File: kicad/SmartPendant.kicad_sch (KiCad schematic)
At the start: 51 parts, among them J1 UART, J2 ST-LINK, J3 Encoder, J5 Display, J6 USB_C_Receptacle_USB2.0_16P, J8 Micro_SD_Card_Det1, Q1 MMBT3904, U1 WEACT BLACKPILL F4X1, U2 AMS1117-3.3, U3 MB85RC256VPNF-G-JNERE1

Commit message: Route some more.
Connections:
- net USR_BTN: now also BTN_USR1.2; no longer BTN_USR1.1
- net at BTN_USR1.SH (B): now also BTN_USR1.1; no longer BTN_USR1.2
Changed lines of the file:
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@@
 		(lib_id "Switch:SW_Push_Shielded")
 		(at 209.55 172.72 0)
+		(mirror y)
 		(unit 1)
 		(exclude_from_sim no)
@@
 		(dnp no)
 		(property "Reference" "BTN_USR1"
-			(at 214.7316 164.0459 0)
+			(at 204.3684 164.0459 0)
 			(effects
 				(font
@@
 		)
 		(property "Value" "SPST"
-			(at 220.091 166.7891 0)
+			(at 199.009 166.7891 0)
 			(effects
 				(font

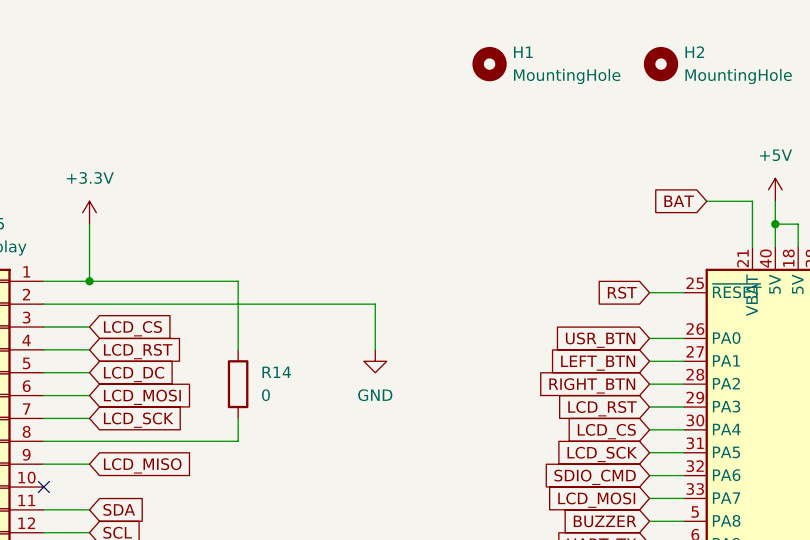
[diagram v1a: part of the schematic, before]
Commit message: Add GND test point.
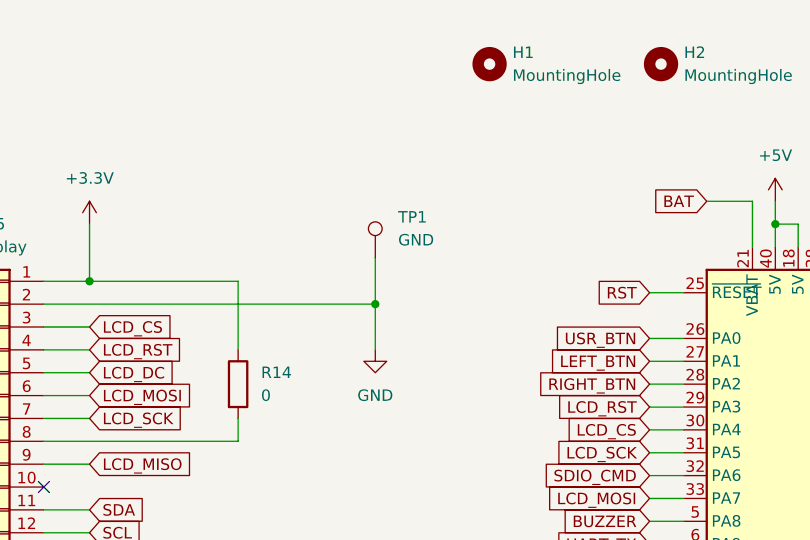
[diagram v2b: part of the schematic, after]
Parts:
- added TP1: GND, TestPoint:TestPoint_Keystone_5000-5004_Miniature, symbol Connector:TestPoint
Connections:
- net GND: now also TP1.1
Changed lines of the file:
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@@
 	)
 	(junction
+		(at 67.31 49.53)
+		(diameter 0)
+		(color 0 0 0 0)
+	)
+	(junction
 		(at 241.3 166.37)
 		(diameter 0)
@@
 	(wire
 		(pts
+			(xy 67.31 44.45) (xy 67.31 49.53)
+		)
+		(stroke
+			(width 0)
+			(type default)
+		)
+	)
+	(wire
+		(pts
 			(xy 241.3 165.1) (xy 241.3 166.37)
 		)
@@
 					(unit 1)
 				)
+			)
+		)
+	)
+	(symbol
+		(lib_id "Connector:TestPoint")
+		(at 67.31 44.45 0)
+		(unit 1)
+		(exclude_from_sim no)
+		(in_bom yes)
+		(on_board yes)
+		(dnp no)
+		(fields_autoplaced yes)
+		(property "Reference" "TP1"
+			(at 69.85 39.8779 0)
+			(effects
+				(font
+					(size 1.27 1.27)
+				)
+				(justify left)
+			)
+		)
+		(property "Value" "GND"
+			(at 69.85 42.4179 0)
+			(effects
+				(font
+					(size 1.27 1.27)
+				)
+				(justify left)
+			)
+		)
+		(property "Footprint" "TestPoint:TestPoint_Keystone_5000-5004_Miniature"
+			(at 72.39 44.45 0)
+			(effects
+				(font
+					(size 1.27 1.27)
+				)
+				(hide yes)
+			)
+		)
+		(property "Datasheet" "~"
+			(at 72.39 44.45 0)
+			(effects
+				(font
+					(size 1.27 1.27)
+				)
+				(hide yes)
+			)
+		)
+		(property "Description" "test point"
+			(at 67.31 44.45 0)
+			(effects
+				(font
+					(size 1.27 1.27)
+				)
+				(hide yes)
+			)
+		)
+		(pin "1"
+		)
+		(instances
+			(project ""
+				(path "/78cb6519-38e9-49e2-a9df-0cb5fdb5035f"
+					(reference "TP1")
+					(unit 1)
+				)

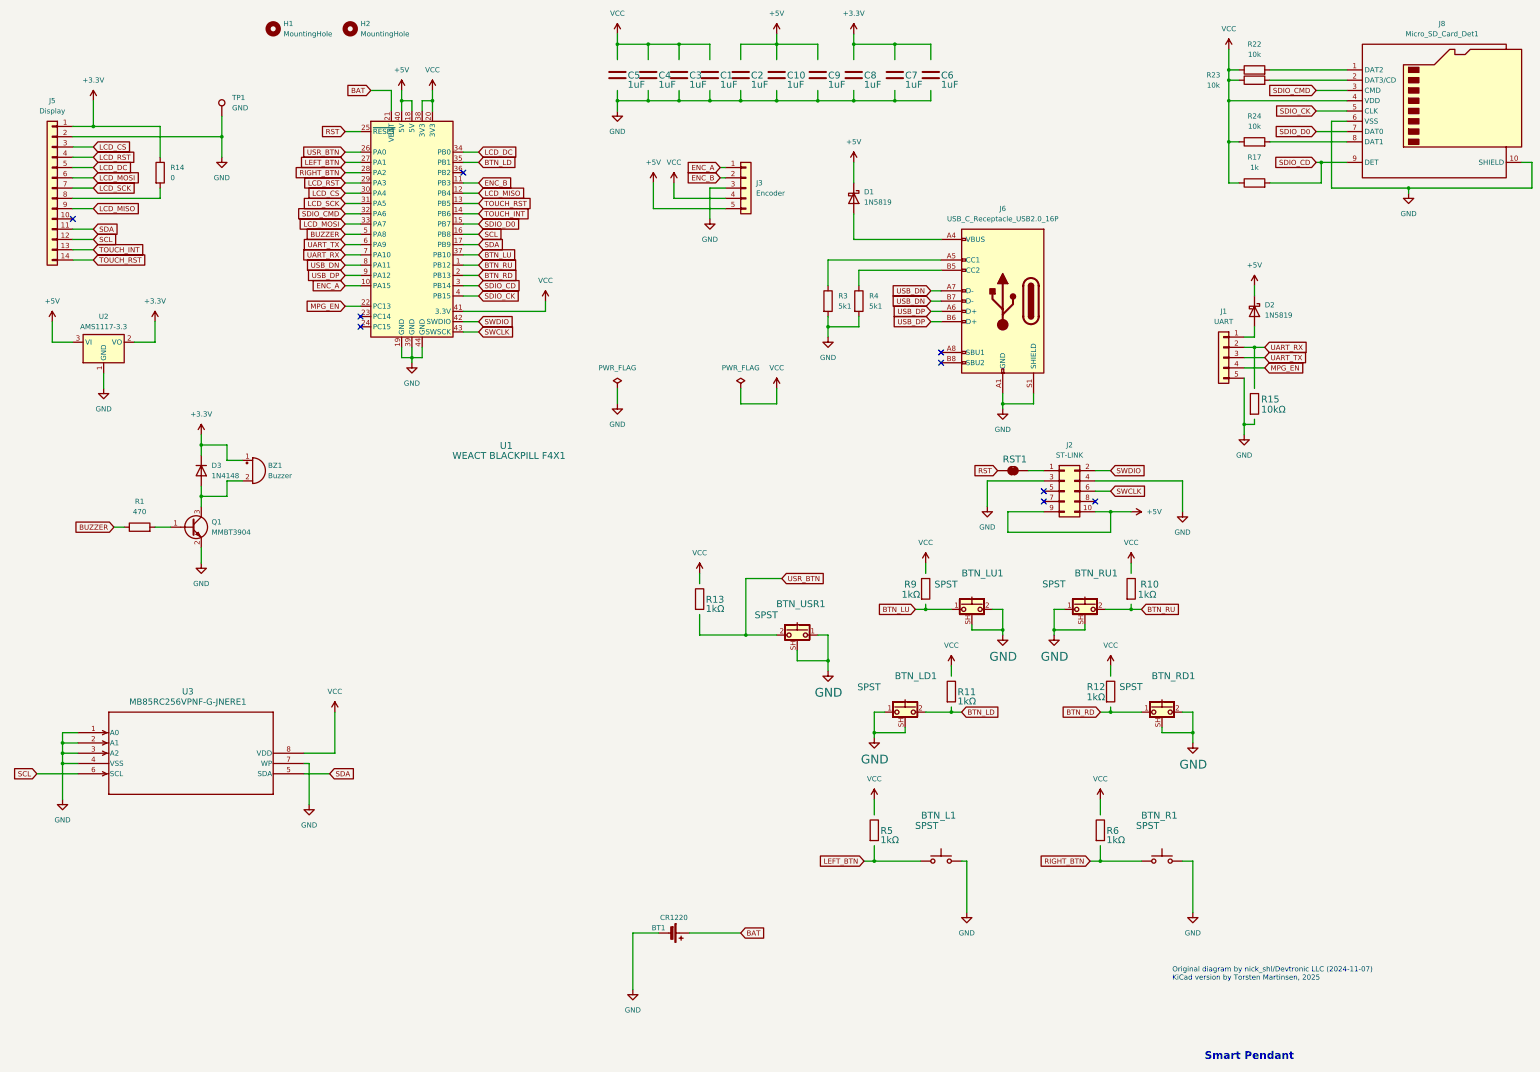
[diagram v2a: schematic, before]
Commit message: Use resistor array; make references consecutive.
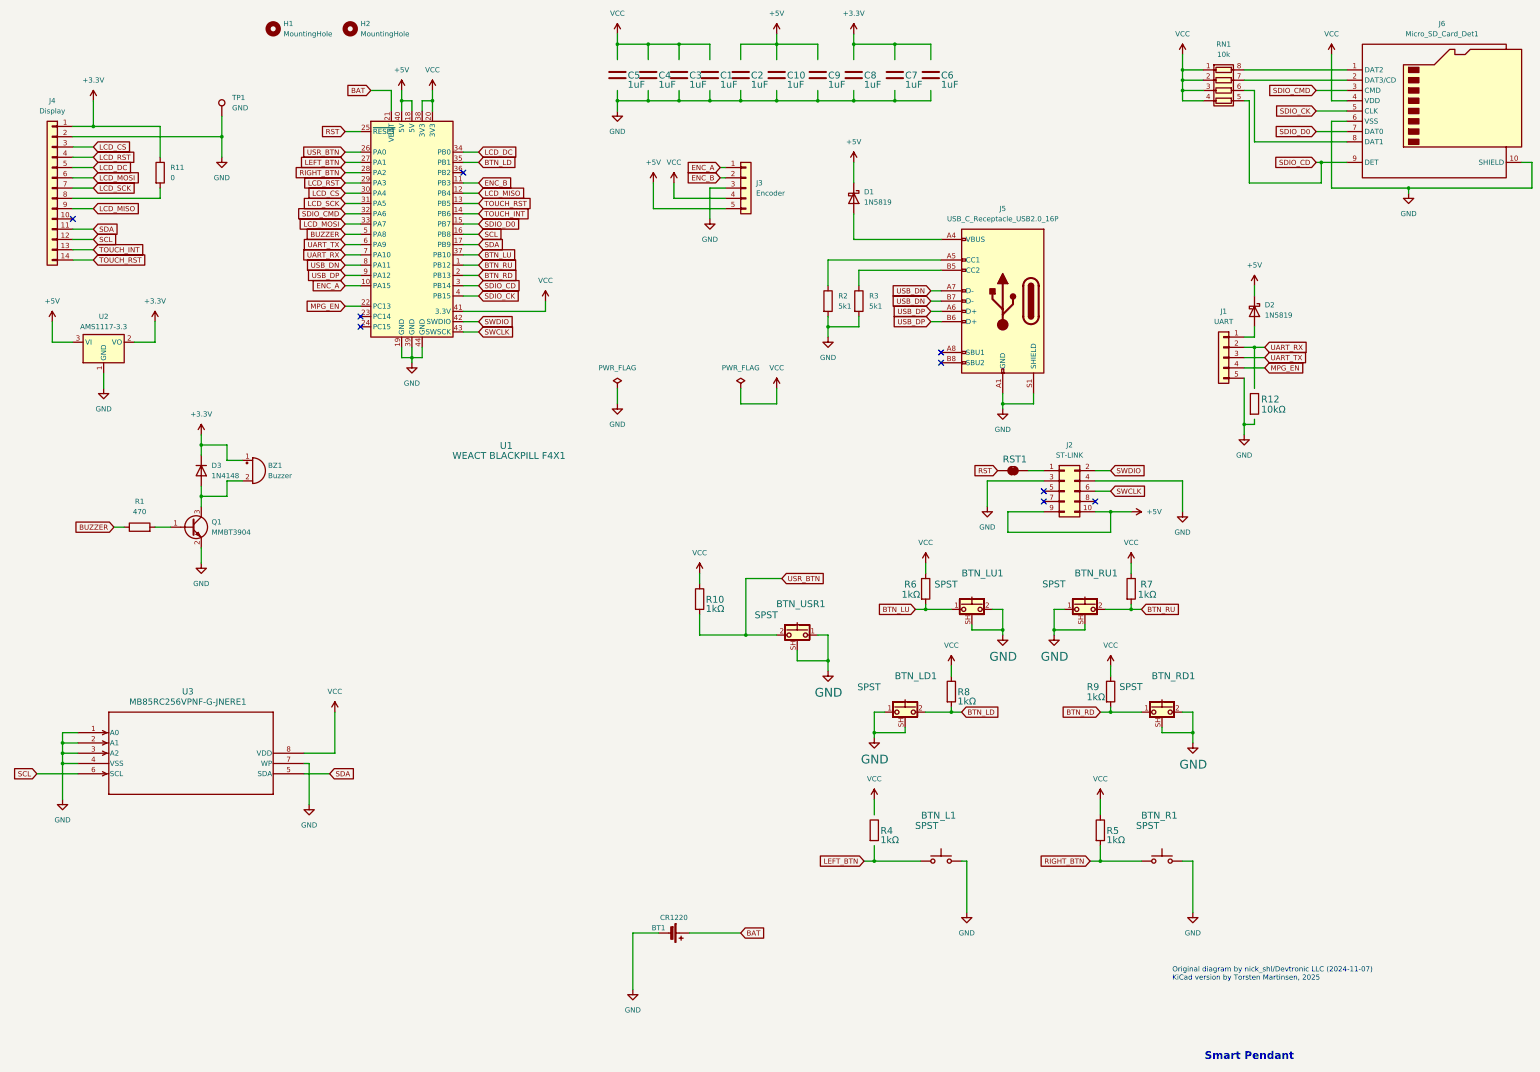
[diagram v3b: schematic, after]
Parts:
- removed R17: 1k, PCM_Resistor_SMD_AKL:R_0603_1608Metric, symbol Device:R
- removed R22, R23, R24: 10k, PCM_Resistor_SMD_AKL:R_0603_1608Metric, symbol Device:R
- added RN1: 10k, PCM_Resistor_SMD_AKL:R_Array_Concave_4x0603, symbol Device:R_Pack04
- renumbered J5 to J4, J6 to J5, J8 to J6, R13 to R10, R14 to R11, R15 to R12, R3 to R2, R4 to R3, R5 to R4, R6 to R5, R9 to R6, R10 to R7, R11 to R8, R12 to R9
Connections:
- net BTN_LD: now also R8.2
- net BTN_LU: now also R6.2
- net BTN_RD: now also R9.2
- net BTN_RU: now also R7.2
- net RIGHT_BTN: now also R5.2
- net SDIO_CD: now also RN1.5 (R4.2)
- net USR_BTN: now also R10.2
- net VCC: now also R10.1, R5.1, R6.1, R7.1, R8.1, R9.1, RN1.1 (R1.1), RN1.2 (R2.1), RN1.3 (R3.1), RN1.4 (R4.1)
- net at J6.2 (DAT3/CD): now also RN1.7 (R2.2)
- net at J6.8 (DAT1): now also RN1.6 (R3.2)
- net at J6.1 (DAT2): now also RN1.8 (R1.2)

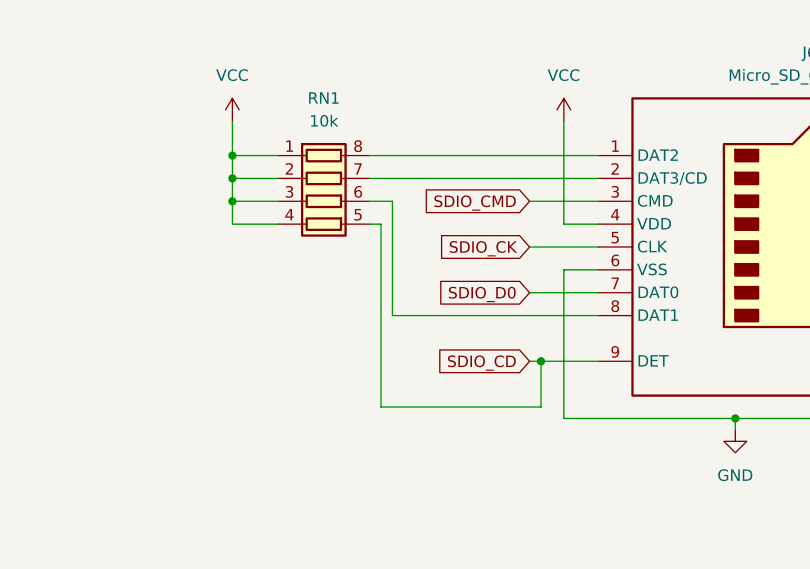
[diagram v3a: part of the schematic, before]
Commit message: Use dual SD-card footprint.
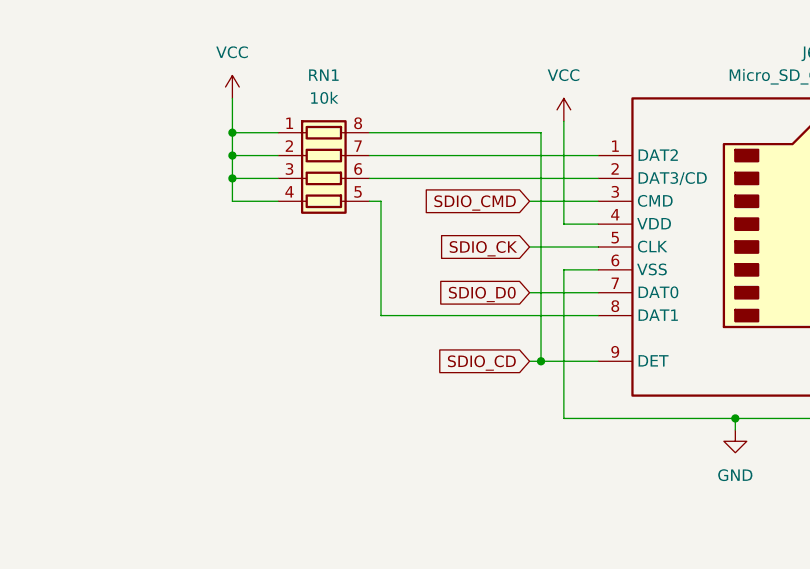
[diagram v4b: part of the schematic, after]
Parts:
- J6: footprint Custom:J_SD_Card-micro_socket_A -> Custom:J_SD_Card-micro_dual
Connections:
- net SDIO_CD: now also RN1.8 (R1.2); no longer RN1.5 (R4.2)
- net at J6.8 (DAT1): now also RN1.5 (R4.2); no longer RN1.6 (R3.2)
- net at J6.2 (DAT3/CD): now also RN1.6 (R3.2); no longer RN1.7 (R2.2)
- net at J6.1 (DAT2): now also RN1.7 (R2.2); no longer RN1.8 (R1.2)
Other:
- moved on the sheet: RN1
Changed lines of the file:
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@@
 	)
 	(junction
-		(at 304.8 38.1)
+		(at 304.8 35.56)
 		(diameter 0)
 		(color 0 0 0 0)
@@
 	)
 	(junction
-		(at 339.09 55.88)
+		(at 214.63 40.64)
 		(diameter 0)
 		(color 0 0 0 0)
 	)
 	(junction
-		(at 214.63 40.64)
+		(at 35.56 46.99)
 		(diameter 0)
 		(color 0 0 0 0)
 	)
 	(junction
-		(at 35.56 46.99)
+		(at 27.94 204.47)
 		(diameter 0)
 		(color 0 0 0 0)
 	)
 	(junction
-		(at 27.94 204.47)
+		(at 339.09 55.88)
 		(diameter 0)
 		(color 0 0 0 0)
@@
 	)
 	(junction
-		(at 304.8 35.56)
+		(at 304.8 33.02)
 		(diameter 0)
 		(color 0 0 0 0)
@@
 	)
 	(junction
-		(at 304.8 33.02)
+		(at 304.8 30.48)
 		(diameter 0)
 		(color 0 0 0 0)
@@
 	(wire
 		(pts
-			(xy 320.04 40.64) (xy 321.31 40.64)
-		)
-		(stroke
-			(width 0)
-			(type default)
-		)
-	)
-	(wire
-		(pts
 			(xy 30.48 62.23) (xy 35.56 62.23)
 		)
@@
 	(wire
 		(pts
-			(xy 304.8 33.02) (xy 304.8 35.56)
+			(xy 304.8 30.48) (xy 304.8 33.02)
 		)
 		(stroke
@@
 	(wire
 		(pts
+			(xy 321.31 38.1) (xy 321.31 50.8)
+		)
+		(stroke
+			(width 0)
+			(type default)
+		)
+	)
+	(wire
+		(pts
 			(xy 97.79 58.42) (xy 101.6 58.42)
 		)
@@
 	(wire
 		(pts
+			(xy 339.09 55.88) (xy 345.44 55.88)
+		)
+		(stroke
+			(width 0)
+			(type default)
+		)
+	)
+	(wire
+		(pts
 			(xy 97.79 66.04) (xy 101.6 66.04)
 		)
@@
 	(wire
 		(pts
-			(xy 304.8 29.21) (xy 304.8 33.02)
+			(xy 304.8 26.67) (xy 304.8 30.48)
 		)
 		(stroke
@@
 	(wire
 		(pts
-			(xy 304.8 38.1) (xy 304.8 40.64)
+			(xy 304.8 35.56) (xy 304.8 38.1)
 		)
 		(stroke
@@
 	(wire
 		(pts
-			(xy 304.8 38.1) (xy 309.88 38.1)
+			(xy 304.8 35.56) (xy 309.88 35.56)
 		)
 		(stroke
@@
 	(wire
 		(pts
-			(xy 304.8 35.56) (xy 309.88 35.56)
+			(xy 304.8 33.02) (xy 309.88 33.02)
 		)
 		(stroke
@@
 	(wire
 		(pts
-			(xy 322.58 38.1) (xy 322.58 50.8)
-		)
-		(stroke
-			(width 0)
-			(type default)
-		)
-	)
-	(wire
-		(pts
 			(xy 217.17 172.72) (xy 217.17 179.07)
 		)
@@
 	(wire
 		(pts
-			(xy 304.8 35.56) (xy 304.8 38.1)
+			(xy 304.8 33.02) (xy 304.8 35.56)
 		)
 		(stroke
@@
 	(wire
 		(pts
+			(xy 320.04 30.48) (xy 339.09 30.48)
+		)
+		(stroke
+			(width 0)
+			(type default)
+		)
+	)
+	(wire
+		(pts
 			(xy 30.48 67.31) (xy 35.56 67.31)
 		)
@@
 	(wire
 		(pts
-			(xy 321.31 60.96) (xy 339.09 60.96)
-		)
-		(stroke
-			(width 0)
-			(type default)
-		)
-	)
-	(wire
-		(pts
 			(xy 236.22 196.85) (xy 228.6 196.85)
 		)
@@
 	(wire
 		(pts
-			(xy 320.04 38.1) (xy 322.58 38.1)
-		)
-		(stroke
-			(width 0)
-			(type default)
-		)
-	)
-	(wire
-		(pts
 			(xy 190.5 59.69) (xy 191.77 59.69)
 		)
@@
 	(wire
 		(pts
-			(xy 304.8 33.02) (xy 309.88 33.02)
+			(xy 304.8 30.48) (xy 309.88 30.48)
 		)
 		(stroke
@@
 	(wire
 		(pts
-			(xy 322.58 50.8) (xy 345.44 50.8)
-		)
-		(stroke
-			(width 0)
-			(type default)
-		)
-	)
-	(wire
-		(pts
-			(xy 339.09 60.96) (xy 339.09 55.88)
-		)
-		(stroke
-			(width 0)
-			(type default)
-		)
-	)
-	(wire
-		(pts
-			(xy 304.8 40.64) (xy 309.88 40.64)
+			(xy 304.8 38.1) (xy 309.88 38.1)
 		)
 		(stroke
@@
 	(wire
 		(pts
-			(xy 339.09 55.88) (xy 345.44 55.88)
+			(xy 104.14 38.1) (xy 109.22 38.1)
 		)
 		(stroke
@@
 	(wire
 		(pts
-			(xy 104.14 38.1) (xy 109.22 38.1)
+			(xy 114.3 40.64) (xy 111.76 40.64)
 		)
 		(stroke
@@
 	(wire
 		(pts
-			(xy 114.3 40.64) (xy 111.76 40.64)
+			(xy 339.09 30.48) (xy 339.09 55.88)
 		)
 		(stroke
@@
 	(wire
 		(pts
+			(xy 320.04 38.1) (xy 321.31 38.1)
+		)
+		(stroke
+			(width 0)
+			(type default)
+		)
+	)
+	(wire
+		(pts
 			(xy 337.82 43.18) (xy 345.44 43.18)
 		)
@@
 	(wire
 		(pts
+			(xy 321.31 50.8) (xy 345.44 50.8)
+		)
+		(stroke
+			(width 0)
+			(type default)
+		)
+	)
+	(wire
+		(pts
 			(xy 287.02 191.77) (xy 294.64 191.77)
 		)
@@
 	(wire
 		(pts
-			(xy 321.31 40.64) (xy 321.31 60.96)
-		)
-		(stroke
-			(width 0)
-			(type default)
-		)
-	)
-	(wire
-		(pts
 			(xy 325.12 104.14) (xy 320.04 104.14)
 		)
@@
 	(symbol
 		(lib_id "power:VCC")
-		(at 304.8 29.21 0)
+		(at 304.8 26.67 0)
 		(unit 1)
 		(exclude_from_sim no)
@@
 		(fields_autoplaced yes)
 		(property "Reference" "#PWR033"
-			(at 304.8 33.02 0)
+			(at 304.8 30.48 0)
 			(effects
 				(font
@@
 		)
 		(property "Value" "VCC"
-			(at 304.8 24.13 0)
+			(at 304.8 21.59 0)
 			(effects
 				(font
@@
 		)
 		(property "Footprint" ""
-			(at 304.8 29.21 0)
+			(at 304.8 26.67 0)
 			(effects
 				(font
@@
 		)
 		(property "Datasheet" ""
-			(at 304.8 29.21 0)
+			(at 304.8 26.67 0)
 			(effects
 				(font
@@
 		)
 		(property "Description" "Power symbol creates a global label with name \"VCC\""
-			(at 304.8 29.21 0)
+			(at 304.8 26.67 0)
 			(effects
 				(font
@@
 	(symbol
 		(lib_id "Device:R_Pack04")
-		(at 314.96 38.1 270)
+		(at 314.96 35.56 270)
 		(unit 1)
 		(exclude_from_sim no)
@@
 		(fields_autoplaced yes)
 		(property "Reference" "RN1"
-			(at 314.96 26.67 90)
+			(at 314.96 24.13 90)
 			(effects
 				(font
@@
 		)
 		(property "Value" "10k"
-			(at 314.96 29.21 90)
+			(at 314.96 26.67 90)
 			(effects
 				(font
@@
 		)
 		(property "Footprint" "PCM_Resistor_SMD_AKL:R_Array_Concave_4x0603"
-			(at 314.96 45.085 90)
+			(at 314.96 42.545 90)
 			(effects
 				(font
@@
 		)
 		(property "Datasheet" "~"
-			(at 314.96 38.1 0)
+			(at 314.96 35.56 0)
 			(effects
 				(font
@@
 		)
 		(property "Description" "4 resistor network, parallel topology"
-			(at 314.96 38.1 0)
+			(at 314.96 35.56 0)
 			(effects
 				(font
@@
 			)
 		)
-		(property "Footprint" "Custom:J_SD_Card-micro_socket_A"
+		(property "Footprint" "Custom:J_SD_Card-micro_dual"
 			(at 420.37 25.4 0)
 			(effects

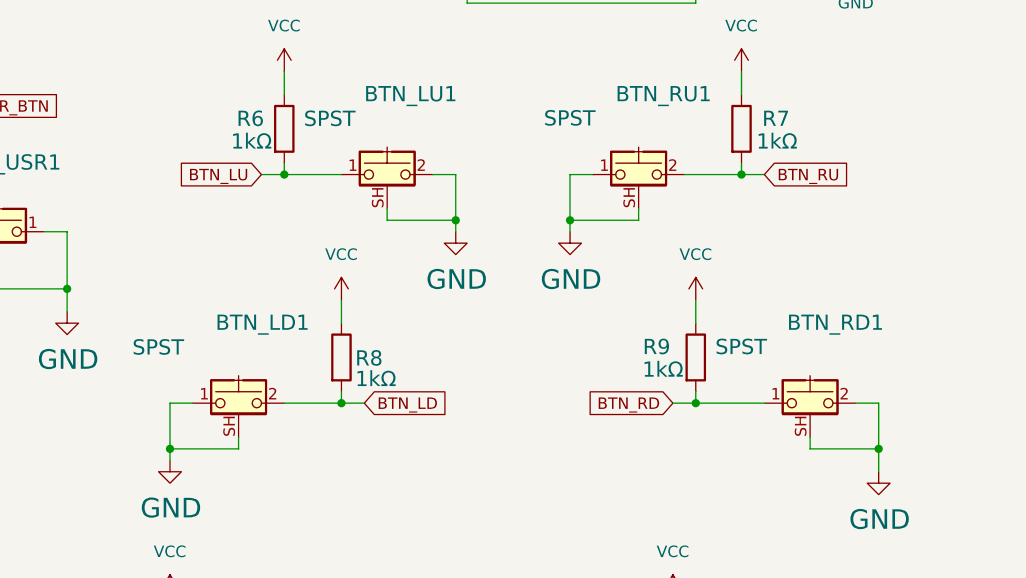
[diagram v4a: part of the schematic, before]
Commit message: Add missing SD card pad. Swap left/right side buttons.
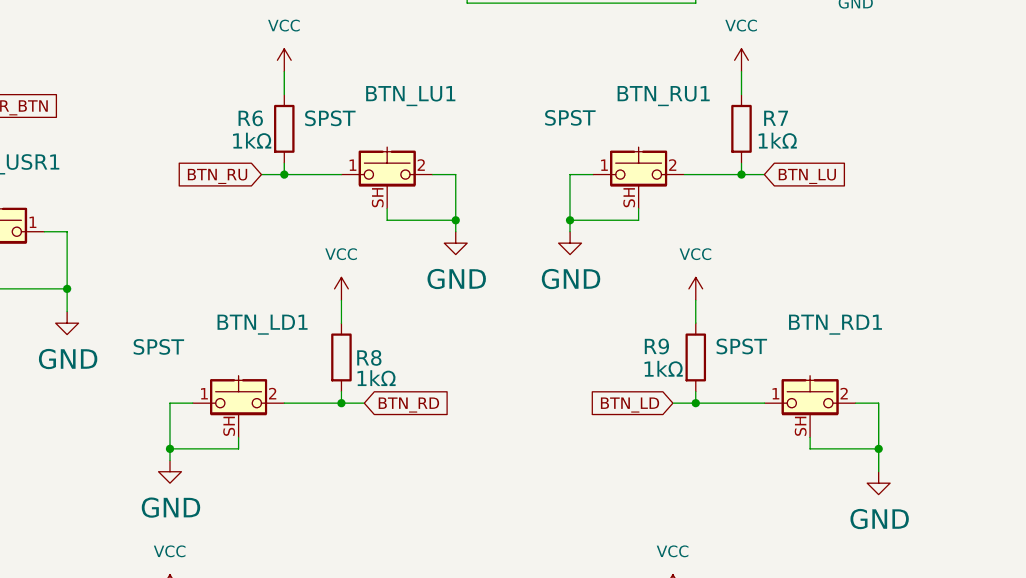
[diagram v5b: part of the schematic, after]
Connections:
- net BTN_LD: now also BTN_RD1.1, R9.2; no longer BTN_LD1.2, R8.2
- net BTN_LU: now also BTN_RU1.2, R7.2; no longer BTN_LU1.1, R6.2
- net BTN_RD: now also BTN_LD1.2, R8.2; no longer BTN_RD1.1, R9.2
- net BTN_RU: now also BTN_LU1.1, R6.2; no longer BTN_RU1.2, R7.2
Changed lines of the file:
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@@
 		)
 	)
-	(global_label "BTN_LD"
+	(global_label "BTN_RD"
 		(shape input)
 		(at 250.19 191.77 0)
@@
 		)
 	)
-	(global_label "BTN_LU"
+	(global_label "BTN_RU"
 		(shape input)
 		(at 238.76 166.37 180)
@@
 		)
 	)
-	(global_label "BTN_RD"
+	(global_label "BTN_LD"
 		(shape input)
 		(at 284.48 191.77 180)
@@
 		)
 	)
-	(global_label "BTN_RU"
+	(global_label "BTN_LU"
 		(shape input)
 		(at 294.64 166.37 0)
